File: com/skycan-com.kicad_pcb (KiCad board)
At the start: 2 copper layers, 50 x 50 mm, 73 parts, among them J1 DF9_25P_1V_PLUG, J2 DF9_25P_1V_SOCKET, J3 DF9_25P_1V_PLUG, J4 DF9_25P_1V_SOCKET, U1 TPS79930, U2 NRF8001, U3 CC112X, U4 UFL, X1 32.768 kHz, X2 16 MHz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

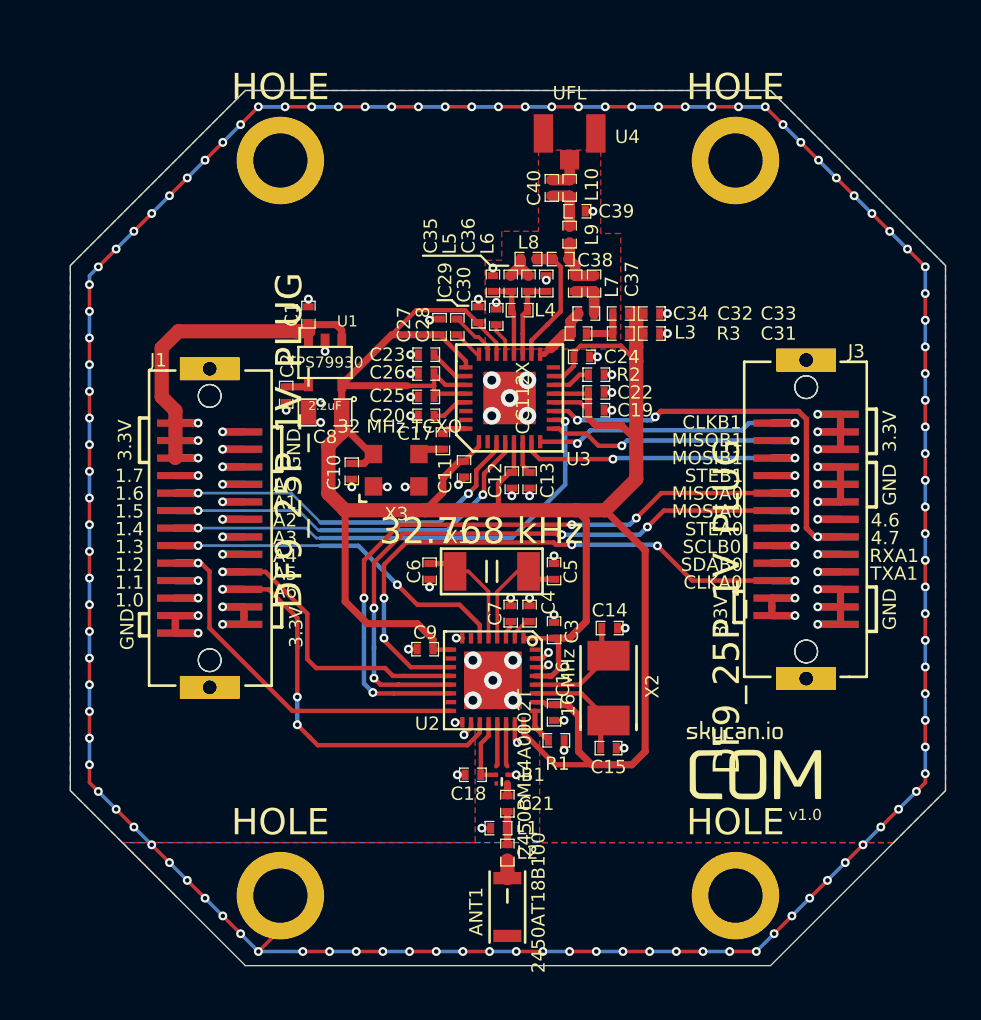
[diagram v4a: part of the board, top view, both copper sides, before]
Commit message: com board via stitching ready
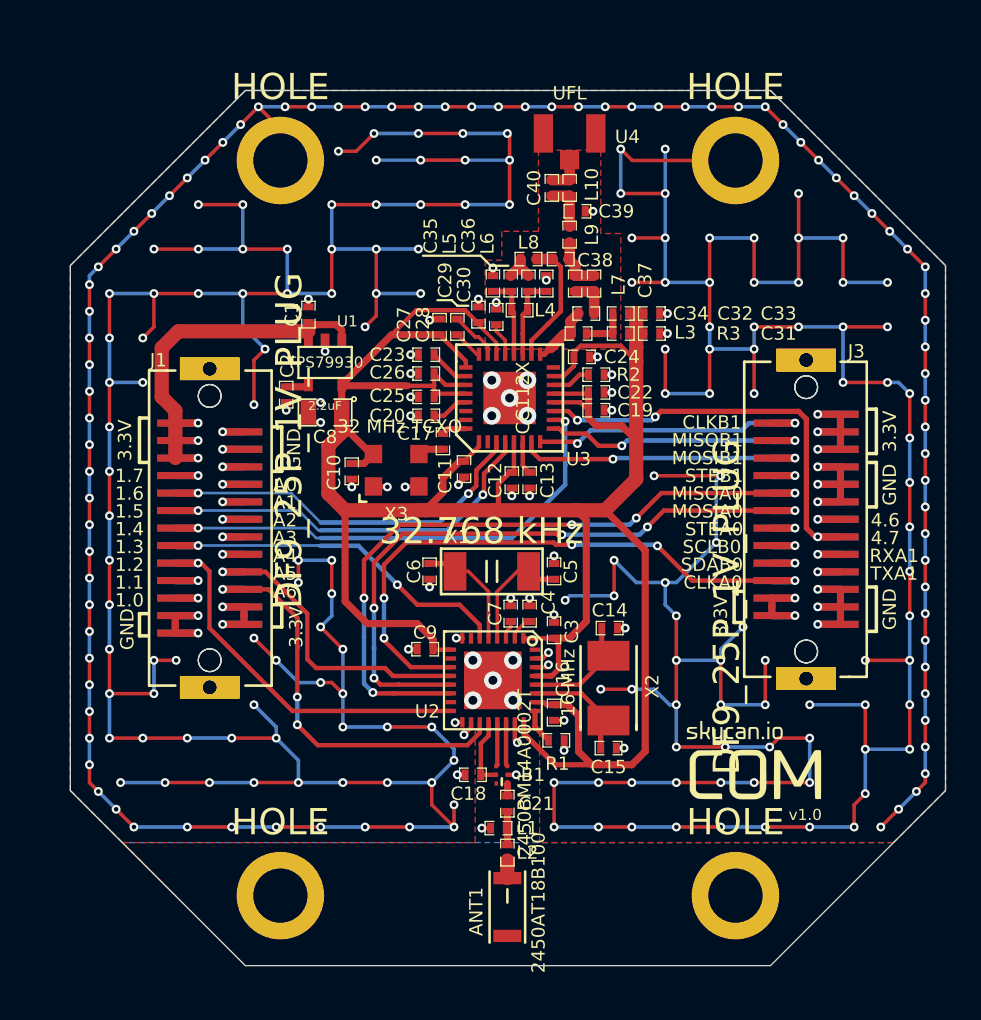
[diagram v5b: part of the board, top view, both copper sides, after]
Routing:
- net GND: track 261.2 -> 626.1 mm, vias 180 -> 314
